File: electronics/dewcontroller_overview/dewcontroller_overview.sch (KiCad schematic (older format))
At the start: 4 parts, among them J1 Barrel_Jack, U1 dewrca, U2 4ch_pwm_board, U3 Teensy3.2 or LC (watch PWM pi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

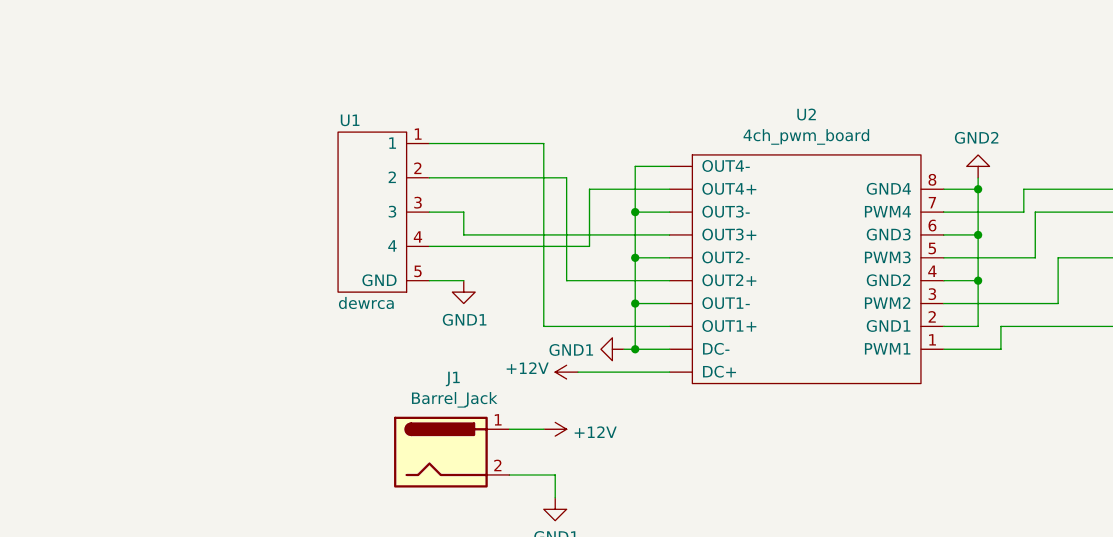
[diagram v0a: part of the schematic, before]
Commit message: Fixed wiring on YYNMOS-4 and RCA board.
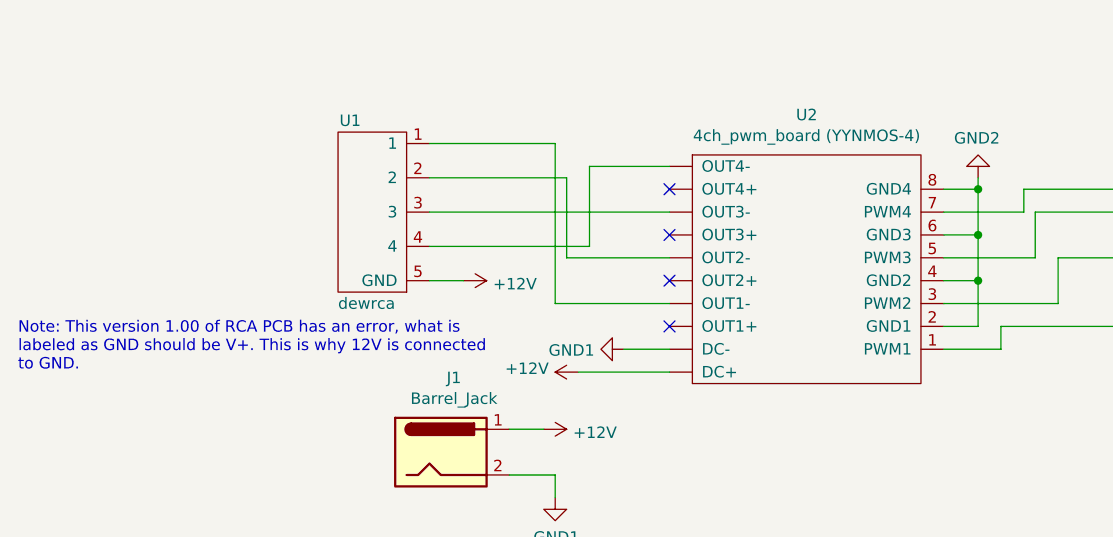
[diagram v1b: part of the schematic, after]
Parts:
- U2: value 4ch_pwm_board -> 4ch_pwm_board (YYNMOS-4)
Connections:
- net +12V: now also U1.5 (GND)
- net GND1: no longer U1.5 (GND)
- no-connect marks 0 -> 4
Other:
- note added: "Note: This version 1.00 of RCA PCB has an error, what is \nlabeled as GND should be V+. This is why 12V is connected\nto GND."
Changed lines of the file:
@@
 P 4950 3700
 F 0 "U2" H 4950 4375 50  0000 C CNN
-F 1 "4ch_pwm_board" H 4950 4284 50  0000 C CNN
+F 1 "4ch_pwm_board (YYNMOS-4)" H 4950 4284 50  0000 C CNN
 F 2 "" H 4950 3700 50  0001 C CNN
 F 3 "" H 4950 3700 50  0001 C CNN
@@
 	1    0    0    -1
 $EndComp
-Wire Wire Line
-	4350 4050 4200 4050
-Wire Wire Line
-	4200 4050 4200 3850
-Wire Wire Line
-	4200 3850 4350 3850
-Wire Wire Line
-	4200 3850 4200 3650
-Wire Wire Line
-	4200 3650 4350 3650
-Connection ~ 4200 3850
-Wire Wire Line
-	4200 3650 4200 3450
-Wire Wire Line
-	4200 3450 4350 3450
-Connection ~ 4200 3650
-Wire Wire Line
-	4200 3450 4200 3250
-Wire Wire Line
-	4200 3250 4350 3250
-Connection ~ 4200 3450
 Wire Wire Line
 	3650 4600 3850 4600
@@
 $EndComp
 Wire Wire Line
-	4150 4050 4200 4050
-Connection ~ 4200 4050
-Wire Wire Line
 	3950 4150 4350 4150
 $Comp
@@
 	0    1    1    0
 $EndComp
-$Comp
-L power:GND1 #PWR0105
-U 1 1 62201743
-P 3450 3750
-F 0 "#PWR0105" H 3450 3500 50  0001 C CNN
-F 1 "GND1" H 3455 3577 50  0000 C CNN
-F 2 "" H 3450 3750 50  0001 C CNN
-F 3 "" H 3450 3750 50  0001 C CNN
-	1    3450 3750
-	1    0    0    -1
-$EndComp
-Wire Wire Line
-	3300 3750 3450 3750
 Wire Wire Line
 	3300 3600 4000 3600
-Wire Wire Line
-	4000 3600 4000 3350
-Wire Wire Line
-	4000 3350 4350 3350
-Wire Wire Line
-	4350 3550 3450 3550
-Wire Wire Line
-	3450 3550 3450 3450
-Wire Wire Line
-	3450 3450 3300 3450
-Wire Wire Line
-	4350 3750 3900 3750
-Wire Wire Line
-	3900 3750 3900 3300
-Wire Wire Line
-	3900 3300 3300 3300
-Wire Wire Line
-	3300 3150 3800 3150
-Wire Wire Line
-	3800 3150 3800 3950
-Wire Wire Line
-	3800 3950 4350 3950
 $Comp
 L power:GND2 #PWR0106
@@
 Text Notes 2300 6150 0    118  ~ 0
 Assembly Note: PWM Board has headers. Solder wires on DewRCA and Teensy side.
+Wire Wire Line
+	4150 4050 4350 4050
+NoConn ~ 4350 3350
+NoConn ~ 4350 3550
+NoConn ~ 4350 3750
+NoConn ~ 4350 3950
+Wire Wire Line
+	4000 3600 4000 3250
+Wire Wire Line
+	4000 3250 4350 3250
+$Comp
+L power:+12V #PWR?
+U 1 1 6226C0A9
+P 3450 3750
+F 0 "#PWR?" H 3450 3600 50  0001 C CNN
+F 1 "+12V" V 3465 3878 50  0000 L CNN
+F 2 "" H 3450 3750 50  0001 C CNN
+F 3 "" H 3450 3750 50  0001 C CNN
+	1    3450 3750
+	0    1    1    0
+$EndComp
+Wire Wire Line
+	3300 3750 3450 3750
+Wire Wire Line
+	3300 3450 4350 3450
+Wire Wire Line
+	3300 3300 3900 3300
+Wire Wire Line
+	3900 3300 3900 3650
+Wire Wire Line
+	3900 3650 4350 3650
+Wire Wire Line
+	3300 3150 3850 3150
+Wire Wire Line
+	3850 3150 3850 3850
+Wire Wire Line
+	3850 3850 4350 3850
+Text Notes 1500 4150 0    50   ~ 0
+Note: This version 1.00 of RCA PCB has an error, what is \nlabeled as GND should be V+. This is why 12V is connected\nto GND.
 $EndSCHEMATC

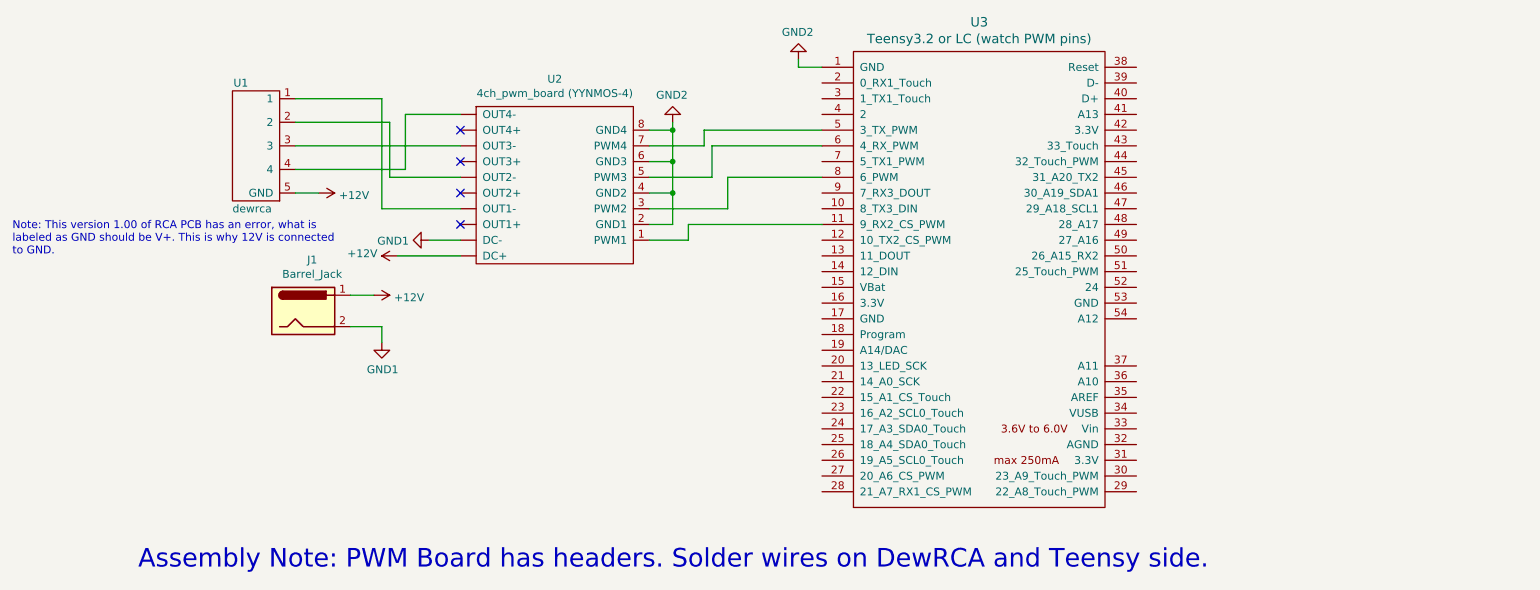
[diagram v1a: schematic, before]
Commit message: Fixed schematic for using relay board instead of pwm board.
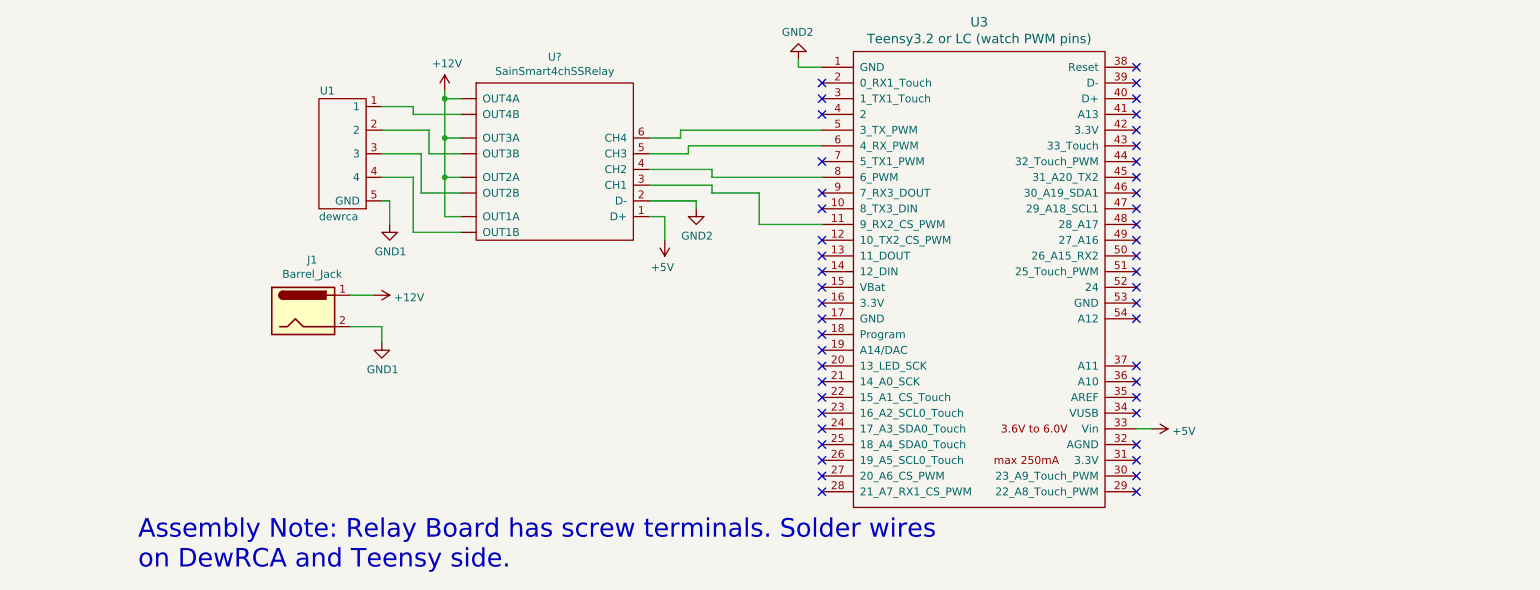
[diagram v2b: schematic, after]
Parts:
- removed U2: 4ch_pwm_board (YYNMOS-4), symbol SST_kicad_sym:4ch_pwm_board
- added U?: SainSmart4chSSRelay, symbol SST_kicad_sym:SainSmart4chSSRelay
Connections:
- net +12V: now also U?.~ (OUT4B); no longer U1.5 (GND)
- net GND1: now also U1.5 (GND)
- net GND2: now also U?.2 (D-)
- net at U3.11 (9_RX2_CS_PWM): now also U?.3 (CH1)
- net +5V: now reaches U3.33 (Vin)
- net +5V: now also U?.1 (D+)
- net at U3.5 (3_TX_PWM): now also U?.6 (CH4)
- net at U3.6 (4_RX_PWM): now also U?.5 (CH3)
- net at U3.8 (6_PWM): now also U?.4 (CH2)
- net at U1.1: now also U?.~ (OUT4B)
- net at U1.2: now also U?.~ (OUT4B)
- net at U1.3: now also U?.~ (OUT4B)
- net at U1.4: now also U?.~ (OUT4B)
- no-connect marks 4 -> 48
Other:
- note added: "Assembly Note: Relay Board has screw terminals. Solder wires \non DewRCA and Teensy side."
- note removed: "Assembly Note: PWM Board has headers. Solder wires on DewRCA and Teensy side."
- note removed: "Note: This version 1.00 of RCA PCB has an error, what is \nlabeled as GND should be V+. This is why 12V is connected\nto GND."
- moved on the sheet: U1
